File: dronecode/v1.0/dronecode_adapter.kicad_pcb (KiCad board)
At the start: 2 copper layers, 18 x 27 mm, 61 parts, among them J1 Jumper, J2 Jumper, J3 Jumper, J4 Jumper, X1 JTAG-10

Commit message: Some minor cleanups.
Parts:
- added REF**: via0305, pkl_misc:via0305, F.Cu at (20.6, 47.1)
- added REF**: via0305, pkl_misc:via0305, F.Cu at (37.3, 47.3)
- moved REF** 1.51 mm to (30.3, 47.3)
- moved REF** 1.50 mm to (32.0, 47.3)
- moved REF** 1.05 mm to (35.8, 47.3)
- moved REF** 1.00 mm to (25.0, 47.2)
- moved REF** 1.00 mm to (23.5, 47.2)
- moved REF** 1.00 mm to (26.2, 47.2)
- moved REF** 1.00 mm to (34.2, 47.2)
- moved PH3 0.85 mm to (25.0, 44.9)
- moved REF** 0.45 mm to (28.2, 32.7)
- moved REF** 0.28 mm to (37.2, 20.8)
- moved REF** 0.21 mm to (37.2, 33.8)
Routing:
- net /TX: track 41.0 -> 43.4 mm
- net /TMS/SWDIO: track 26.3 -> 28.3 mm
- net /TCK/SWCLK: track 25.3 -> 26.7 mm
- net VCC: track 27.5 -> 28.9 mm
- net /RX: track 38.1 -> 38.8 mm
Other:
- board size 18 x 27 mm -> 18 x 28 mm
- rule pad_to_mask_clearance: 0.07 -> 0.075
- rule via_min_size: 0.4 -> 0.5
- board text added: "JVCC"
- board text added: "TX RX DIO CLK GND"
- board text added: "UVCC"

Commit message: Minor cleanup.
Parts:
- added REF**: via0305, pkl_misc:via0305, F.Cu at (26.0, 41.5)
- moved REF** 0.45 mm to (33.8, 47.3)
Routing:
- net /TMS/SWDIO: track 28.3 -> 25.0 mm, vias 3 -> 2
- net /TX: track 43.4 -> 42.6 mm, vias 3 -> 2
- net /RX: track 38.8 -> 38.1 mm, vias 3 -> 2
- net /TCK/SWCLK: track 26.7 -> 26.8 mm, vias 3 -> 2

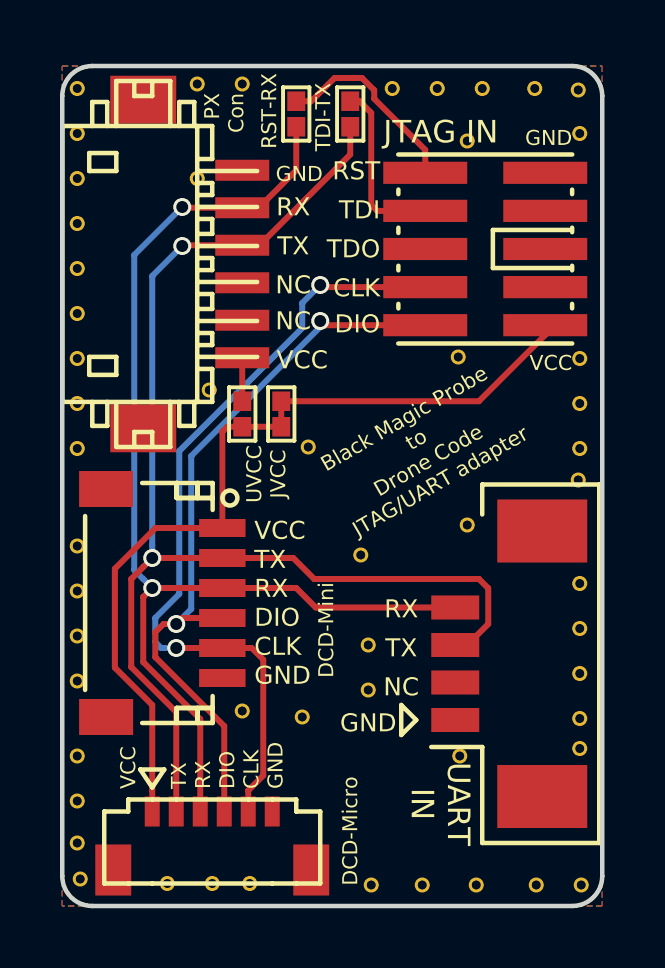
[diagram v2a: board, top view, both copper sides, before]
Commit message: Some name corrections.
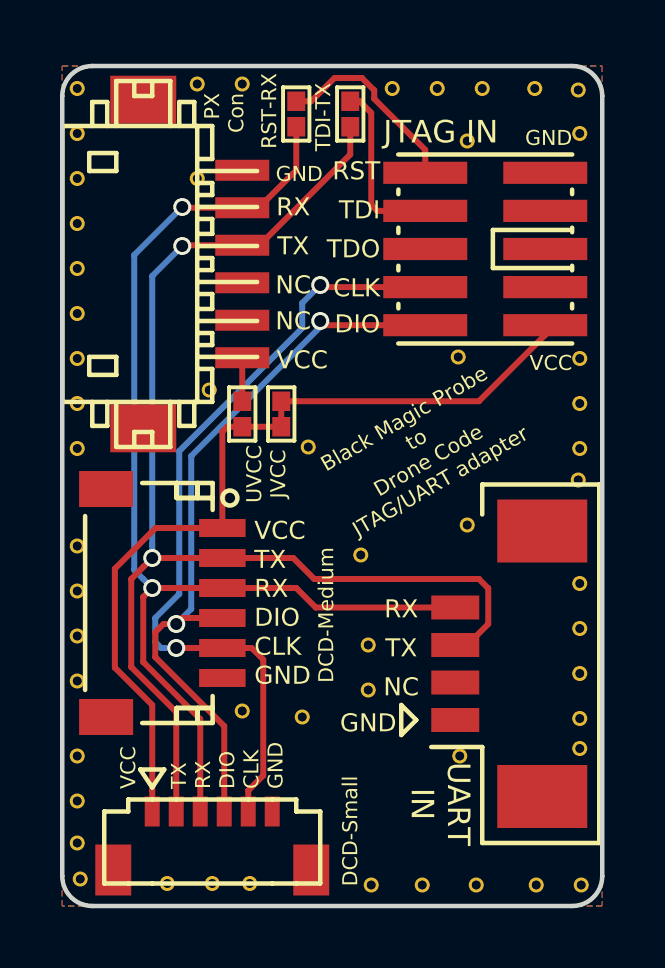
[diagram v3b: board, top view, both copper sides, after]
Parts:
- PH2: value SH06B-SRSS-TB -> SM06B-SRSS-TB
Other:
- board text added: "DCD-Medium"
- board text added: "DCD-Small"
- board text removed: "DCD-Micro"
- board text removed: "DCD-Mini"
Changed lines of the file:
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@@
 (kicad_pcb (version 4) (host pcbnew 4.0.1-4.201602132031+6195~38~ubuntu14.04.1-stable)
   (general
-    (links 79)
+    (links 80)
     (no_connects 0)
     (area 19.924999 19.924999 38.075001 48.075001)
@@
       (effects (font (size 1 1) (thickness 0.15)))
     )
-    (fp_text value SH06B-SRSS-TB (at 0 4.2625 270) (layer F.Fab) hide
+    (fp_text value SM06B-SRSS-TB (at 0 4.2625 270) (layer F.Fab) hide
       (effects (font (size 1 1) (thickness 0.15)))
     )
@@
       (rotate (xyz 0 0 0))
     )
+    (model walter/conn_df13/df13a-6p-125h.wrl
+      (at (xyz 0 0 0))
+      (scale (xyz 1 1 1))
+      (rotate (xyz 0 0 0))
+    )
   )
   (module pkl_logos:1b2_Logo_SilkS_10mm (layer B.Cu)
@@
     (effects (font (size 0.5 0.5) (thickness 0.125)) (justify right))
   )
-  (gr_text DCD-Mini (at 28.8 38.8 90) (layer F.SilkS)
+  (gr_text DCD-Medium (at 28.8 38.3 90) (layer F.SilkS)
     (effects (font (size 0.5 0.5) (thickness 0.125)))
   )
@@
     (effects (font (size 0.75 0.75) (thickness 0.1875)) (justify left))
   )
-  (gr_text DCD-Micro (at 29.6 45.5 90) (layer F.SilkS)
+  (gr_text DCD-Small (at 29.6 45.5 90) (layer F.SilkS)
     (effects (font (size 0.5 0.5) (thickness 0.125)))
   )
